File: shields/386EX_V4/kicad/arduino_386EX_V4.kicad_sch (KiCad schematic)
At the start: 46 parts, among them J1 Conn_01x02_Pin, J2 JTAG, J3 Conn_01x04_Pin, J4 Conn_01x04_Pin, J5 Conn_01x04_Pin, J6 SERIAL0, J9 WP Jumper, U1 AT24CS01-STUM, U11 I386EX_PQFP, U2 ULN2003A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

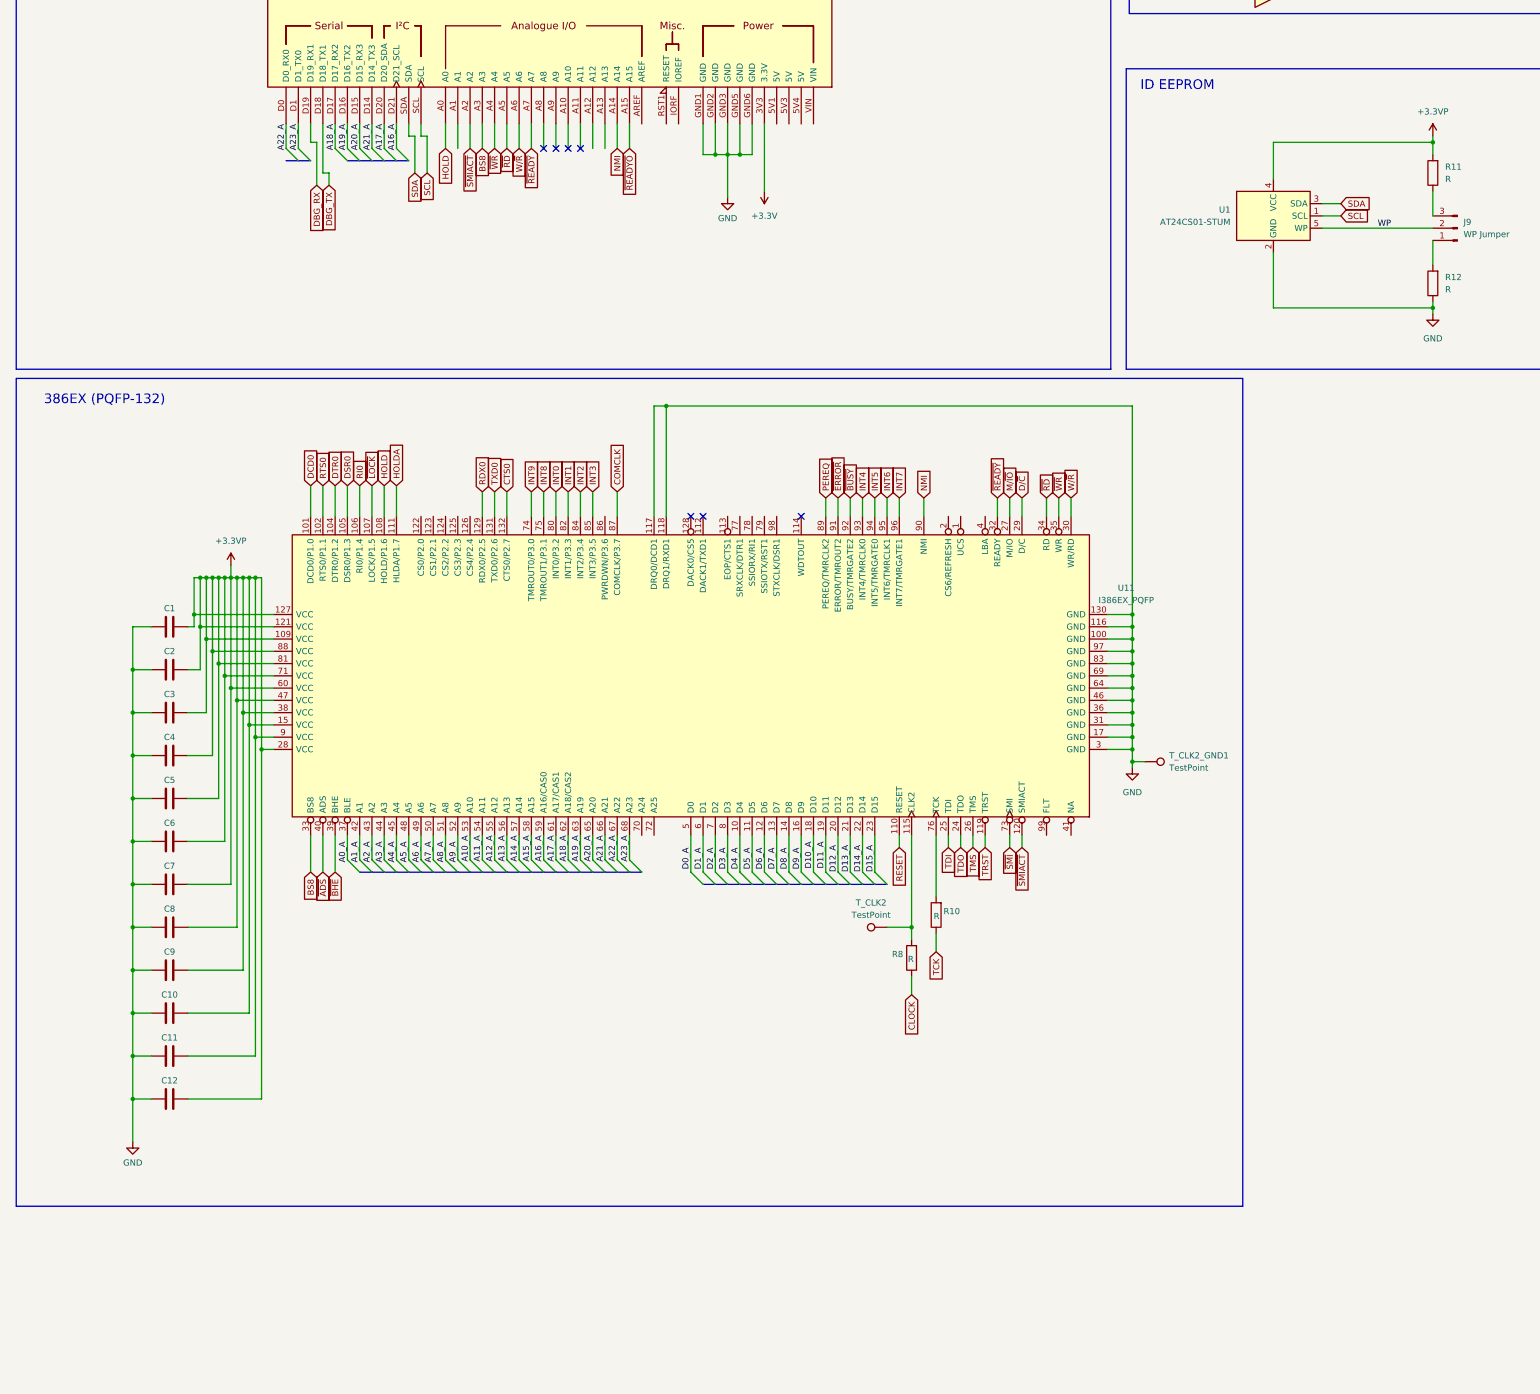
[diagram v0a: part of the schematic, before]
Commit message: Revert added files in shields/386ex_v4/
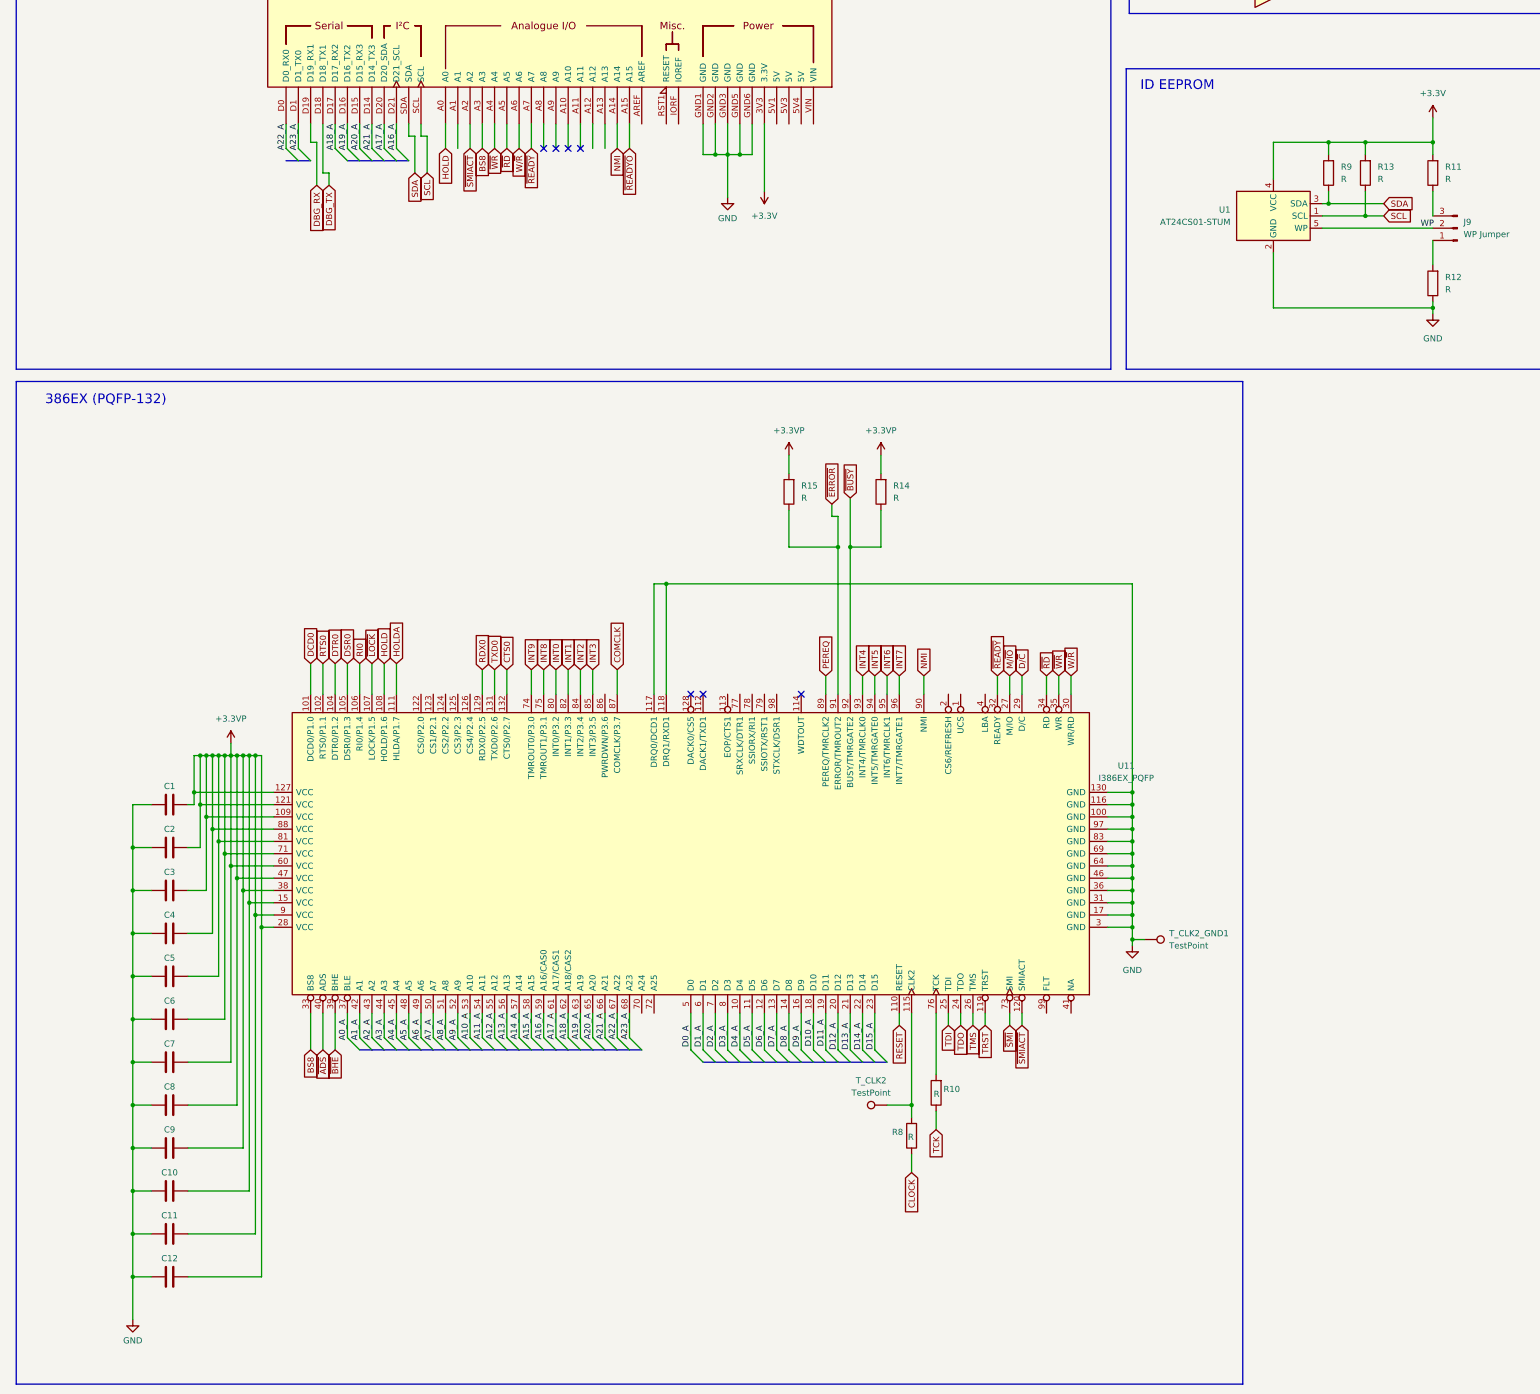
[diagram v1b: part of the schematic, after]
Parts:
- added R13, R14, R15, R9: R, Resistor_SMD:R_0603_1608Metric_Pad0.98x0.95mm_HandSolder, symbol Device:R
- added unit 6 of U3
- added unit 5 of U3
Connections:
- net +3.3V: now also R11.2, U1.4 (VCC), R13.2, R9.2
- net +3.3VP: now also R14.2, R15.2; no longer R11.2, U1.4 (VCC)
- net RD: now also U3.10; no longer U3.10
- net SCL: now also R13.1
- net SDA: now also R9.1
- net WR: now also U3.12; no longer U3.12
- net ~{BUSY}: now also R14.1
- net ~{ERROR}: now also R15.1
- net ~{RD}: now also U3.11; no longer U3.11
- net ~{WR}: now also U3.13; no longer U3.13
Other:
- moved on the sheet: C1, C10, C11, C12, C2, C3, C4, C5, C6, C7, C8, C9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
